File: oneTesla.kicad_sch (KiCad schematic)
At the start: 41 parts, among them IC1 74HCT14, IC2 74HCT74, IC3 UCC37321P, IC4 UCC37321P, IC6 78L05, J1 IEC C6, J110 Jumper 110V, J2 PE/CHASSIS, P1 PRIMARIO A, P2 PRIMARIO B, Q1 FGA60N65SMD, Q2 FGA60N65SMD, T1 1:1:1, T3 1:300

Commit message: docs(schematic): record per-reference review constraints without topology changes
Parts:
- C1, C2, C3, C4, C5, C6: Footprint_Status Pacote padronizado; conferir componente adquirido -> REVIEW: Disco P5, furos/pads inventariados; dielétrico/tens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
- C10: Footprint_Status Pacote padronizado; conferir componente adquirido -> REVIEW: Pendente MPN: pitch real 3.556 versus nome 5; corpo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
- C11, C12: Footprint_Status Selecao D30/P10 snap-in; medir capacitores 1000uF adquirido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 -> REVIEW: REPROVADO envelope D30: centros distam 26.035 mm, s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
- C13, C8, C9: Footprint_Status Pacote padronizado; conferir componente adquirido -> REVIEW: Pendente MPN: pitch real 2.54 versus nome 3.50; F02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
- CPR1: Footprint_Status PROVISORIO: CDE 940C30S68K-F 68nF/3000V, P57.5 selecionado 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 -> REVIEW: CDE 940C30S68K-F: corpo 46x19 e fio 1 mm conferem c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
- D1, D2: Footprint_Status 1N4148 DO-35 THT: confirmado; passo selecionado 7.62 mm -> REVIEW: DO35 P7.62 genérico; conferir MPN e faixa de cátodo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
- D4: Footprint_Status KBU6G proposto: +1 AC2 AC3 -4, passo 5.08 mm; confirmar cod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 -> REVIEW: KBU6G fabricante indefinido; pads seguem GBU4S orig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
- F1: Footprint_Status Clipes para fusivel 5x20 mm propostos; confirmar modelo rea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 -> REVIEW: Pads ±5.08/±10.16, furos1.1938; fab herdado desloca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
- FB1: Footprint_Status HFBR-2521ETZ pad 1 OUT,2 GND,3 VCC,4 RL,5/8 retencao NC; va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 -> HFBR-2521ETZ: geometria Broadcom AV02-3283EN p4, pitch 2.54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
- IC1, IC2: Footprint_Status DIP-14, passo 2.54 mm, fileiras 7.62 mm: confirmado pelo la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 -> REVIEW: DIP14 P2.54 W7.62; furo0.8128 pad1.6; MPN/sufixo e 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
- IC3, IC4: Footprint_Status DIP-8, passo 2.54 mm, fileiras 7.62 mm: confirmado pelo lay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 -> REVIEW: PDIP8 P2.54 W7.62 coerente; soquete exato pendente;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
- IC6: Footprint_Status 78L05/78L15 TO-92: OUT1 GND2 IN3; conferir fabricante e suf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 -> REVIEW: REVISAR: footprint chamado Inline tem pads triangul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
- J1: Footprint_Status PROVISORIO: entrada IEC C6; geometria e numeracao propostas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 -> REVIEW: IEC C6 sem MPN; trilha de rede invade furo mecânico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
- J110: Footprint_Status Jumper de fio P10.16 mm estimado do layout; confirmar dimen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 -> REVIEW: P10.16 furo2.2; jumper deve ter corrente/isolação e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
- J2: Footprint_Status Ponto PE/chassis M3 proposto; conferir fixacao e continuida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 -> REVIEW: Furo3.2 M3 pad5.1; cobre só0.2059 da borda; resistê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
- P1, P2: Footprint_Status PROVISORIO: terminal M6 e pad de solda no mesmo net; confir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 -> REVIEW: Nome M6 incompatível com furo2.2: geometria para fi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
- PS1: Footprint_Status Datasheet 15W-BL V1.0 p11; 47.5x28.5mm enclosure reference,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 -> REVIEW: Pitch42.5/7.8/22.6 confere desenho de referência; f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
- Q1, Q2: Footprint_Status FGA60N65SMD TO-3P-3: G1 C2 E3, passo 5.45 mm; conferir altu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 -> REVIEW: Pitch5.45 confere onsemi; furo1.4986 perto do envel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
- R1: Footprint_Status Pacote padronizado; conferir componente adquirido -> REVIEW: REPROVADO envelope: corpo declarado 25 mm, furos di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
- R2, R3, R4: Footprint_Status Pacote padronizado; conferir componente adquirido -> REVIEW: DIN0207 P7.62 coerente genericamente; conferir potê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
- R5, R6: Footprint_Status Pacote padronizado; conferir componente adquirido -> REVIEW: Pendente MPN 0.5 W: pitch real 10.16, nome 12.70; f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
- T1: Footprint_Status PROVISORIO: bobina GDT 6 pinos, grade 8.89 mm estimada do l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 -> REVIEW: P0584 original renumerado; pads fora de courtyard g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
- T3: Footprint_Status PROVISORIO: CT 1:300 com 2 pinos do secundario, P12.70 esti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 -> REVIEW: P12.7 furo1.27; dimensões/core/relação real/fase/bu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
- Z1, Z2: Footprint_Status Pacote padronizado; conferir componente adquirido -> REVIEW: DNP no esquema mas não no PCB; F08. Pitch real14.73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

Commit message: fix(footprints): restore HFBR geometry and recenter custom body markings
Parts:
- C10: footprint oneTesla:CP_Radial_D12.5mm_P5.00mm -> oneTesla:CP_D12.5_P3.556_ReviewPending
- C11, C12: footprint oneTesla:CP_Radial_D30.0mm_P10.00mm_SnapIn -> oneTesla:CP_D30_P10.16_ReviewPending
- C13, C8, C9: footprint oneTesla:CP_Radial_D8.0mm_P3.50mm -> oneTesla:CP_D8_P2.54_ReviewPending
- R1: footprint oneTesla:R_Axial_Power_L25.0mm_W6.4mm_P30.48mm -> oneTesla:R_L25_P22.86_INCOMPATIBLE
- R5, R6: footprint oneTesla:R_Axial_DIN0309_L9.0mm_D3.2mm_P12.70mm_Horizontal -> oneTesla:R_L9_P10.16_ReviewPending
- Z1, Z2: footprint oneTesla:D_DO-201AD_P15.24mm_Horizontal -> oneTesla:D_DO201AD_P14.732_ReviewPending
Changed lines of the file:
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@@
       )
     )
-    (property "Footprint" "oneTesla:CP_Radial_D8.0mm_P3.50mm"
+    (property "Footprint" "oneTesla:CP_D8_P2.54_ReviewPending"
       (at 168.91 168.91 0)
       (hide yes)
@@
       )
     )
-    (property "Footprint" "oneTesla:R_Axial_DIN0309_L9.0mm_D3.2mm_P12.70mm_Horizontal"
+    (property "Footprint" "oneTesla:R_L9_P10.16_ReviewPending"
       (at 384.81 74.93 0)
       (hide yes)
@@
       )
     )
-    (property "Footprint" "oneTesla:CP_Radial_D8.0mm_P3.50mm"
+    (property "Footprint" "oneTesla:CP_D8_P2.54_ReviewPending"
       (at 201.93 222.25 0)
       (hide yes)
@@
       )
     )
-    (property "Footprint" "oneTesla:CP_Radial_D8.0mm_P3.50mm"
+    (property "Footprint" "oneTesla:CP_D8_P2.54_ReviewPending"
       (at 133.35 168.91 0)
       (hide yes)
@@
       )
     )
-    (property "Footprint" "oneTesla:CP_Radial_D30.0mm_P10.00mm_SnapIn"
+    (property "Footprint" "oneTesla:CP_D30_P10.16_ReviewPending"
       (at 355.6 74.93 0)
       (hide yes)
@@
       )
     )
-    (property "Footprint" "oneTesla:R_Axial_DIN0309_L9.0mm_D3.2mm_P12.70mm_Horizontal"
+    (property "Footprint" "oneTesla:R_L9_P10.16_ReviewPending"
       (at 384.81 120.65 0)
       (hide yes)
@@
       )
     )
-    (property "Footprint" "oneTesla:D_DO-201AD_P15.24mm_Horizontal"
+    (property "Footprint" "oneTesla:D_DO201AD_P14.732_ReviewPending"
       (at 322.58 74.93 90)
       (hide yes)
@@
       )
     )
-    (property "Footprint" "oneTesla:CP_Radial_D12.5mm_P5.00mm"
+    (property "Footprint" "oneTesla:CP_D12.5_P3.556_ReviewPending"
       (at 144.78 219.71 0)
       (hide yes)
@@
       )
     )
-    (property "Footprint" "oneTesla:R_Axial_Power_L25.0mm_W6.4mm_P30.48mm"
+    (property "Footprint" "oneTesla:R_L25_P22.86_INCOMPATIBLE"
       (at 46.99 73.66 90)
       (hide yes)
@@
       )
     )
-    (property "Footprint" "oneTesla:D_DO-201AD_P15.24mm_Horizontal"
+    (property "Footprint" "oneTesla:D_DO201AD_P14.732_ReviewPending"
       (at 322.58 120.65 90)
       (hide yes)
@@
       )
     )
-    (property "Footprint" "oneTesla:CP_Radial_D30.0mm_P10.00mm_SnapIn"
+    (property "Footprint" "oneTesla:CP_D30_P10.16_ReviewPending"
       (at 355.6 120.65 0)
       (hide yes)

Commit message: fix(pcb): enlarge board and space capacitor bank with verified routing
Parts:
- C11, C12: Footprint_Status REVIEW: REPROVADO envelope D30: centros distam 26.035 mm, s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 -> D30/P10.16 envelope retained; centers35mm, body gap5mm, boa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
- R1: footprint oneTesla:R_L25_P22.86_INCOMPATIBLE -> oneTesla:R_L25_P30.48_Provisional; Footprint_Status REVIEW: REPROVADO envelope: corpo declarado 25 mm, furos di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 -> PROVISIONAL body25mm; lead spacing30.48mm (2.74mm each side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
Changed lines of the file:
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@@
       )
     )
-    (property "Footprint_Status" "REVIEW: REPROVADO envelope D30: centros distam 26.035 mm, sobreposição 3.965 mm; F03. Pitch 10.16, MPN desconhecido"
+    (property "Footprint_Status" "D30/P10.16 envelope retained; centers35mm, body gap5mm, board edge min5mm after enlargement. Exact MPN/ripple/tolerance NOT verified."
       (at 355.6 74.93 0)
       (hide yes)
@@
       )
     )
-    (property "Footprint" "oneTesla:R_L25_P22.86_INCOMPATIBLE"
+    (property "Footprint" "oneTesla:R_L25_P30.48_Provisional"
       (at 46.99 73.66 90)
       (hide yes)
@@
       )
     )
-    (property "Footprint_Status" "REVIEW: REPROVADO envelope: corpo declarado 25 mm, furos distam 22.86 mm; silk/fab deslocados 15.24 mm; F02"
+    (property "Footprint_Status" "PROVISIONAL body25mm; lead spacing30.48mm (2.74mm each side). Confirm exact MPN, lead forming and thermal clearance."
       (at 46.99 73.66 90)
       (hide yes)
@@
       )
     )
-    (property "Footprint_Status" "REVIEW: REPROVADO envelope D30: centros distam 26.035 mm, sobreposição 3.965 mm; F03. Pitch 10.16, MPN desconhecido"
+    (property "Footprint_Status" "D30/P10.16 envelope retained; centers35mm, body gap5mm, board edge min5mm after enlargement. Exact MPN/ripple/tolerance NOT verified."
       (at 355.6 120.65 0)
       (hide yes)

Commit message: fix(cad): preserve geometry and document remaining DRC blockers
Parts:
- Q1, Q2: footprint oneTesla:TO-3P-3_Horizontal_TabDown -> oneTesla:Q_TO3P_ImportedPads_ReviewPending
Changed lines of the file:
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@@
       )
     )
-    (property "Footprint" "oneTesla:TO-3P-3_Horizontal_TabDown"
+    (property "Footprint" "oneTesla:Q_TO3P_ImportedPads_ReviewPending"
       (at 294.64 74.93 0)
       (hide yes)
@@
       )
     )
-    (property "Footprint" "oneTesla:TO-3P-3_Horizontal_TabDown"
+    (property "Footprint" "oneTesla:Q_TO3P_ImportedPads_ReviewPending"
       (at 294.64 120.65 0)
       (hide yes)

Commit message: Atualiza esquema, footprints e modelos 3D dos componentes
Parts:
- F1: footprint oneTesla:Fuseholder_Clip-5x20mm_Littelfuse_111_Inline_P20.00x5.00mm_D1.05mm_Horizontal -> oneTesla:Fuseholder_Idall_AS-06_5x20mm_P20.20mm_Horizontal; Assembly_Notes Lista do kit: 4A. Serigrafia antiga menciona 10A; nao assum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 -> Porta-fusivel AS-06 5x20mm, 2 terminais; 1 AC_L, 2 AC_L_FUS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; Footprint_Status REVIEW: Pads ±5.08/±10.16, furos1.1938; fab herdado desloca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 -> AS-06 Idall0179: P20.2±0.3mm, corpo26x9.6mm; furo1.8/pad3.2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
- IC6: value 78L05 -> L7805CV; footprint oneTesla:TO-92_Inline -> oneTesla:TO-220-3_Vertical; symbol oneTesla:78L05 -> oneTesla:L7805; Assembly_Notes (none) -> L7805CV TO-220: 1 +15V, 2 GND, 3 +5V; aba metalica ligada a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; Footprint_Status REVIEW: REVISAR: footprint chamado Inline tem pads triangul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 -> TO-220-3 vertical: passo2.54mm, furos1.1mm, pinagem L7805 1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
- J1: value IEC C6 -> 2EDGRC-5.08-02P; footprint oneTesla:IEC_C6_CONFIRMAR -> oneTesla:TerminalBlock_2EDGRC-5.08_1x02_P5.08mm_Horizontal; symbol oneTesla:IEC_C6 -> oneTesla:AC_Input_2EDGRC_2P; Assembly_Notes (none) -> 1 = L; 2 = N. PE externo em J2/CHASSIS, separado de GND e D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; Footprint_Status REVIEW: IEC C6 sem MPN; trilha de rede invade furo mecânico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 -> Passo5.08; modelo STEP recebido; terminal quadrado1mm, furo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
- J2: Assembly_Notes Ponto explicito de ligacao PE ao chassis; inferido da trilh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 -> Entrada PE externa direta ao chassis por J2; J1 possui some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
- P1, P2: footprint oneTesla:Primary_Terminal_M6_CONFIRMAR -> oneTesla:Primary_WirePad_D4.0mm_Drill2.2mm; Assembly_Notes (none) -> Soldar fio do primario diretamente ao pad; furoD2.2mm/padD4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; Footprint_Status REVIEW: Nome M6 incompatível com furo2.2: geometria para fi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 -> Ponto de solda direta do fio do primario: um pad circularD4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
- R1: footprint oneTesla:R_L25_P30.48_Provisional -> oneTesla:R_Axial_Vishay_AC05_L18.0mm_D7.5mm_P23.40mm_Horizontal; Assembly_Notes (none) -> AC05 axial 1k/5W; formar terminais em23.4mm para casar com 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; Footprint_Status PROVISIONAL body25mm; lead spacing30.48mm (2.74mm each side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 -> AC05 corpo18xD7.5mm conforme Vishay28730 p10; P23.4mm medid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
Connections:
- net +15V: now also IC6.1 (IN); no longer IC6.3 (VI)
- net +5V: now also IC6.3 (OUT); no longer IC6.1 (VO)
- net PE: no longer J1.3 (PE)

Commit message: cad(board): converte ICs e passivos para SMD e reduz contorno para 100x100mm
- Esquema: IC1/IC2 SOIC-14, desacoplamento 0805, R5/R6 2512,
  D1/D2 1N4148WS SOD-323, IC6 DPAK, C8/C10/C13 CP_Elec_8x10, C9 1210,
  R1 vertical AC05, R2/R3 1206, R4 DIN0207 THT
- PCB: reposicionamento e roteamento, contorno (31,375;27,05)-(131,375;127,05)mm
- Valores de referência ocultos na PCB
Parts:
- C1, C2, C3, C5, C6: footprint oneTesla:C_Disc_D7.5mm_W2.5mm_P5.00mm -> oneTesla:C_0805_2012Metric_Pad1.18x1.45mm_HandSolder; Footprint_Status REVIEW: Disco P5, furos/pads inventariados; dielétrico/tens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 -> SMD 0805; pads for hand soldering.
- C10: value 680u 35V -> 100u 35V; footprint oneTesla:CP_D12.5_P3.556_ReviewPending -> oneTesla:CP_Elec_8x10; Footprint_Status REVIEW: Pendente MPN: pitch real 3.556 versus nome 5; corpo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 -> Capxon 100uF/35V SMD; standard D8 x H10mm assumed, dimensio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
- C11, C12: footprint oneTesla:CP_D30_P10.16_ReviewPending -> oneTesla:CP_D25_H45_P10.16_ReviewPending; Footprint_Status D30/P10.16 envelope retained; centers35mm, body gap5mm, boa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 -> Ketuo 1000uF 200V, body D25 x H45mm from user image. Existi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
- C13, C8: value 100u 25V -> 100u 35V; footprint oneTesla:CP_D8_P2.54_ReviewPending -> oneTesla:CP_Elec_8x10; Footprint_Status REVIEW: Pendente MPN: pitch real 2.54 versus nome 3.50; F02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 -> GENERIC: standard SMD 8x10mm selected as requested; purchas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
- C9: value 100u 10V -> 100u 35V; footprint oneTesla:CP_D8_P2.54_ReviewPending -> oneTesla:CP_Elec_8x10; Footprint_Status REVIEW: Pendente MPN: pitch real 2.54 versus nome 3.50; F02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 -> GENERIC: standard SMD 8x10mm selected as requested; purchas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
- D1, D2: value 1N4148 -> 1N4148WS; footprint oneTesla:D_DO-35_SOD27_P7.62mm_Horizontal -> oneTesla:D_SOD-323_HandSoldering; Footprint_Status REVIEW: DO35 P7.62 genérico; conferir MPN e faixa de cátodo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 -> 1N4148WS in SOD-323; 1=cathode/2=anode; pads for hand solde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
- IC1, IC2: footprint oneTesla:DIP-14_W7.62mm_Socket_LongPads -> oneTesla:SOIC-14_3.9x8.7mm_P1.27mm; Footprint_Status REVIEW: DIP14 P2.54 W7.62; furo0.8128 pad1.6; MPN/sufixo e 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 -> SMD footprint: oneTesla:SOIC-14_3.9x8.7mm_P1.27mm
- IC6: value L7805CV -> MC7805BDTRKG; footprint oneTesla:TO-220-3_Vertical -> oneTesla:TO-252-3_TabPin2; Assembly_Notes L7805CV TO-220: 1 +15V, 2 GND, 3 +5V; aba metalica ligada a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 -> 1=+15V, 2/tab=GND, 3=+5V. Provide appropriate ground copper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; Footprint_Status TO-220-3 vertical: passo2.54mm, furos1.1mm, pinagem L7805 1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 -> DPAK/TO-252 per onsemi MC7800 ordering table; MC7805BDTRKG 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
- R1: footprint oneTesla:R_Axial_Vishay_AC05_L18.0mm_D7.5mm_P23.40mm_Horizontal -> oneTesla:R_Axial_Vishay_AC05_L18.0mm_D7.5mm_P10.16mm_Vertical; Assembly_Notes AC05 axial 1k/5W; formar terminais em23.4mm para casar com 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 -> Vertical body above pad1; body clearance >=3mm in STEP; ass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; Footprint_Status AC05 corpo18xD7.5mm conforme Vishay28730 p10; P23.4mm medid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 -> Vertical manual forming P10.16mm; nominal body18xD7.5mm; ve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
- R2, R3: footprint oneTesla:R_Axial_DIN0207_L6.3mm_D2.5mm_P7.62mm_Horizontal -> oneTesla:R_1206_3216Metric; Footprint_Status REVIEW: DIN0207 P7.62 coerente genericamente; conferir potê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 -> SMD footprint: oneTesla:R_1206_3216Metric
- R5, R6: footprint oneTesla:R_L9_P10.16_ReviewPending -> oneTesla:R_Uniroyal_HV12_2512_P6.60mm; Footprint_Status REVIEW: Pendente MPN 0.5 W: pitch real 10.16, nome 12.70; f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 -> SMD 2512 land pattern, 6.60mm pad pitch; value100k0.5W pres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
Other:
- note added: "AC/IN"

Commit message: cad: amplia jumper 110V e configura regras de fabricacao
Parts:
- J110: footprint oneTesla:J110_WireLink_P10.16mm -> oneTesla:J110_WireLink_P15.24mm; Footprint_Status REVIEW: P10.16 furo2.2; jumper deve ter corrente/isolação e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 -> REVIEW: P15.24 furo2.2; confirmar corrente/isolacao do fio;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
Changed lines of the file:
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@@
 			)
 		)
-		(property "Footprint" "oneTesla:J110_WireLink_P10.16mm"
+		(property "Footprint" "oneTesla:J110_WireLink_P15.24mm"
 			(at 106.68 264.16 0)
 			(hide yes)
@@
 			)
 		)
-		(property "Footprint_Status" "REVIEW: P10.16 furo2.2; jumper deve ter corrente/isolação especificados e intertravamento/rotulagem; nunca selecionar fechado em220"
+		(property "Footprint_Status" "REVIEW: P15.24 furo2.2; confirmar corrente/isolacao do fio; aberto em220V"
 			(at 106.68 264.16 0)
 			(hide yes)

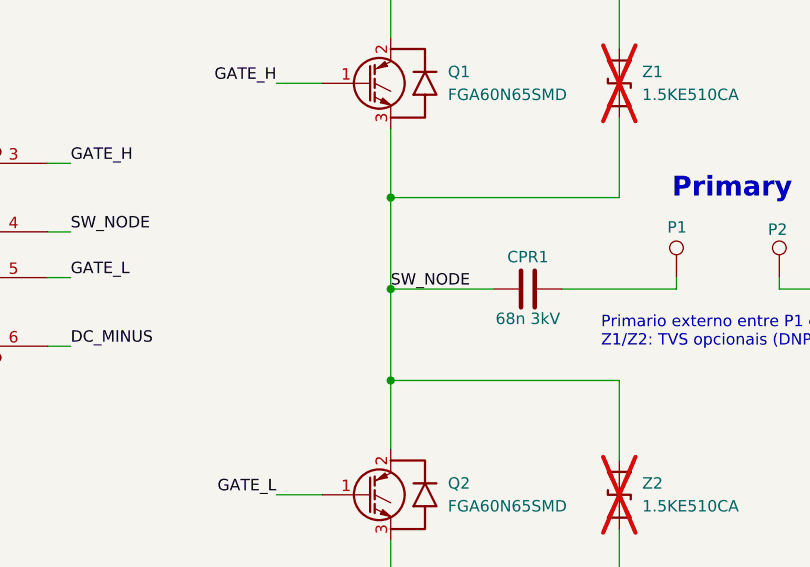
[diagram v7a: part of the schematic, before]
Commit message: feat: finalize ARCSTRIKE rev 1.2 PCB updates
Refine copper zones, restore the T3 primary wire jumper, correct FB1 pads and silkscreen, and add plated fuseholder slots. Include validation reports, previews, and revision backups.
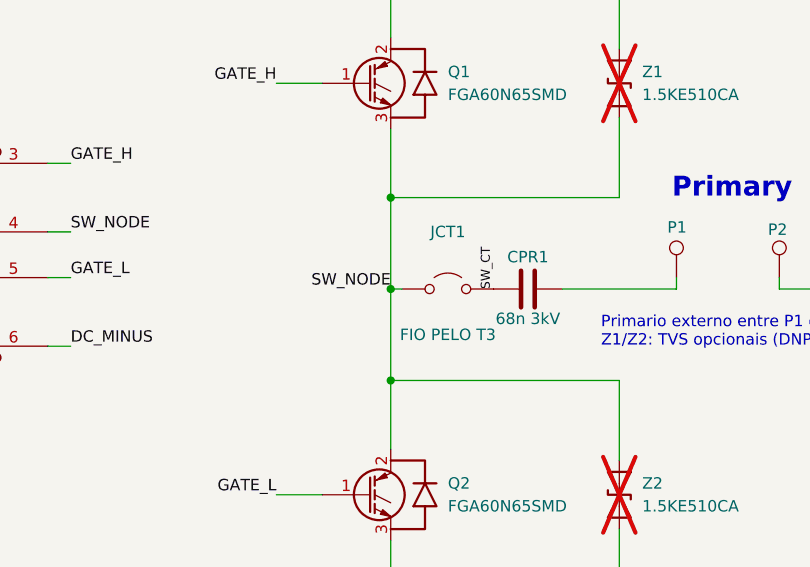
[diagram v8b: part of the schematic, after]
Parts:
- added JCT1: FIO PELO T3, oneTesla:CT_Primary_WireLink_P21.59mm, symbol oneTesla:Jumper
- F1: footprint oneTesla:Fuseholder_Idall_AS-06_5x20mm_P20.20mm_Horizontal -> oneTesla:Fuseholder_Idall_AS-06_5x20mm_Slotted_P22.35mm; Assembly_Notes Porta-fusivel AS-06 5x20mm, 2 terminais; 1 AC_L, 2 AC_L_FUS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 -> Montagem tolerante: terminais acomodados em slots metalizad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; Footprint_Status AS-06 Idall0179: P20.2±0.3mm, corpo26x9.6mm; furo1.8/pad3.2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 -> Adaptacao de montagem AS-06: pad6.0x3.2, slot4.4x1.8, anel 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
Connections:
- net SW_NODE: now also JCT1.1 (A); no longer CPR1.1
- new net SW_CT: CPR1.1, JCT1.2 (B)
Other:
- title: oneTeslaTS - Placa principal / Main board -> ARCSTRIKE - DRSSTC baseada no oneTeslaTS
